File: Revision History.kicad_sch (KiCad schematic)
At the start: 0 parts

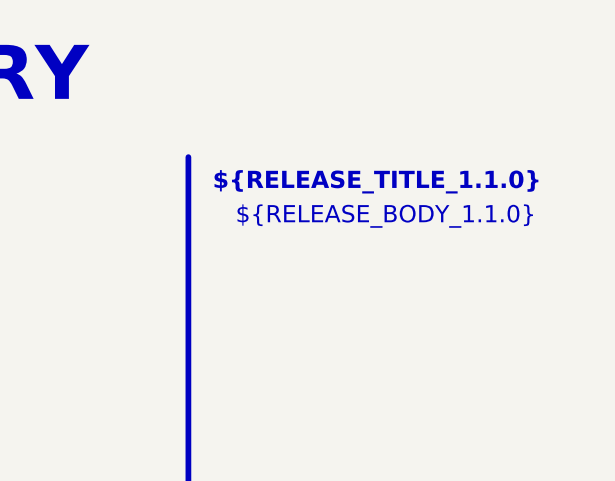
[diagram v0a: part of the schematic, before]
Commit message: fix: improved crystal oscillator layout
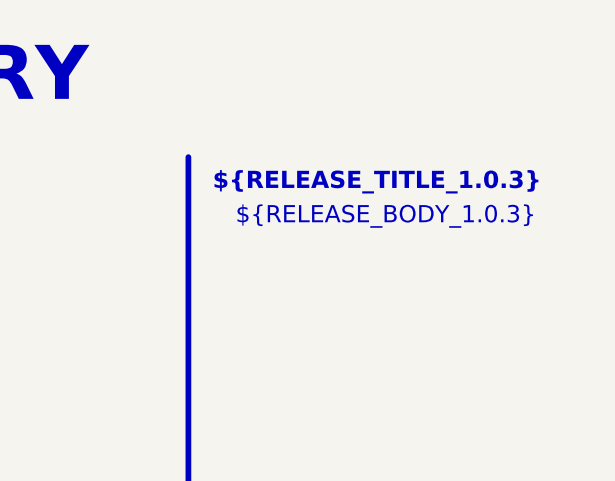
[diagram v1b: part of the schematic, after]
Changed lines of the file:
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@@
 		(company "${COMPANY}")
 	)
-	(text_box "${RELEASE_BODY_1.1.0}"
+	(text_box "${RELEASE_BODY_1.0.3}"
 		(exclude_from_sim no)
 		(at 224.79 35.56 0)
@@
 		(stroke
 			(width -0.0001)
-			(type default)
+			(type solid)
 		)
 		(fill
@@
 		)
 	)
-	(text_box "${RELEASE_TITLE_1.1.0}"
+	(text_box "${RELEASE_TITLE_1.0.3}"
 		(exclude_from_sim no)
 		(at 222.25 31.75 0)
@@
 		(stroke
 			(width -0.0001)
-			(type default)
+			(type solid)
 		)
 		(fill

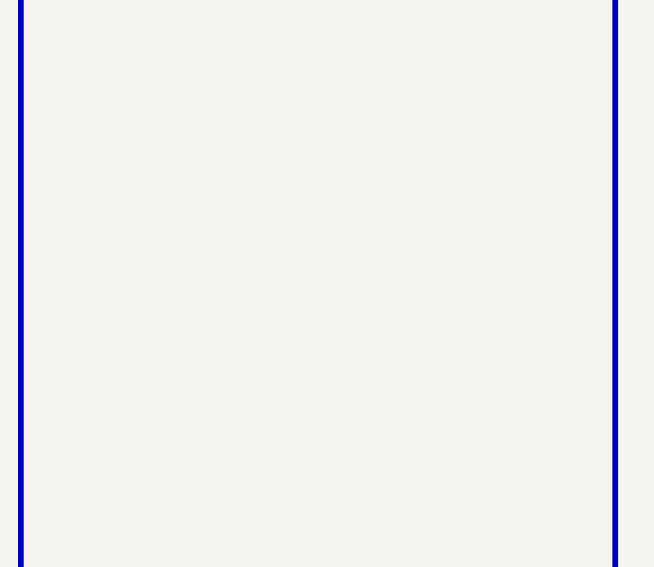
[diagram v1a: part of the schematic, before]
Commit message: fix: add ground pour under uC
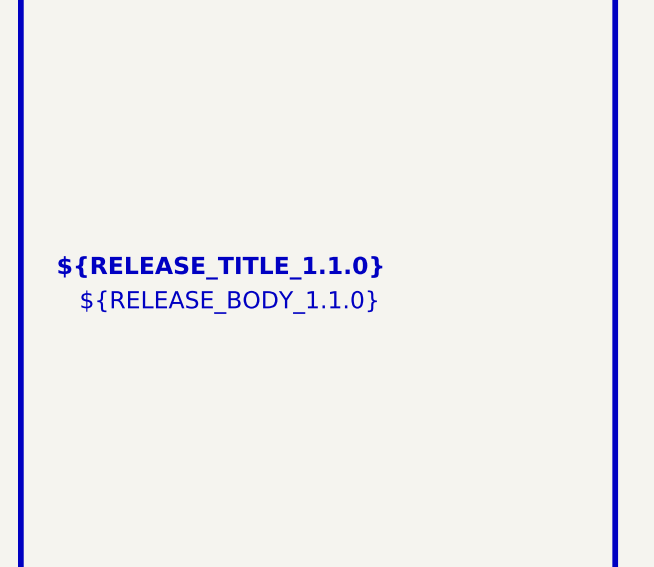
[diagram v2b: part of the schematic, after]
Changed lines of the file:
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@@
+		)
+	)
+	(text_box "${RELEASE_TITLE_1.1.0}"
+		(exclude_from_sim no)
+		(at 25.4 67.31 0)
+		(size 57.15 7.62)
+		(margins 1.4287 1.4287 1.4287 1.4287)
+		(stroke
+			(width -0.0001)
+			(type solid)
+		)
+		(fill
+			(type none)
+		)
+		(effects
+			(font
+				(face "Arial")
+				(size 1.905 1.905)
+				(thickness 0.254)
+				(bold yes)
+			)
+			(justify left top)
 		)
 	)
@@
 		(exclude_from_sim no)
 		(at 26.67 35.56 0)
-		(size 58.42 146.05)
+		(size 58.42 29.21)
 		(margins 1.4287 1.4287 1.4287 1.4287)
 		(stroke
@@
 		)
 		(fill
+			(type none)
+		)
+		(effects
+			(font
+				(face "Arial")
+				(size 1.905 1.905)
+				(color 0 0 0 1)
+			)
+			(justify left top)
+		)
+	)
+	(text_box "${RELEASE_BODY_1.1.0}"
+		(exclude_from_sim no)
+		(at 27.94 71.12 0)
+		(size 58.42 29.21)
+		(margins 1.4287 1.4287 1.4287 1.4287)
+		(stroke
+			(width -0.0001)
+			(type solid)
+		)
+		(fill

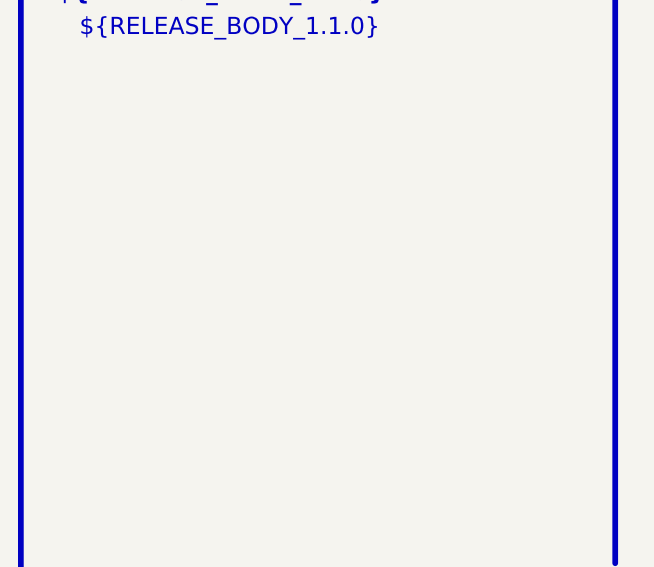
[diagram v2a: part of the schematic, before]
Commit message: fix: circuit schem as one sheet
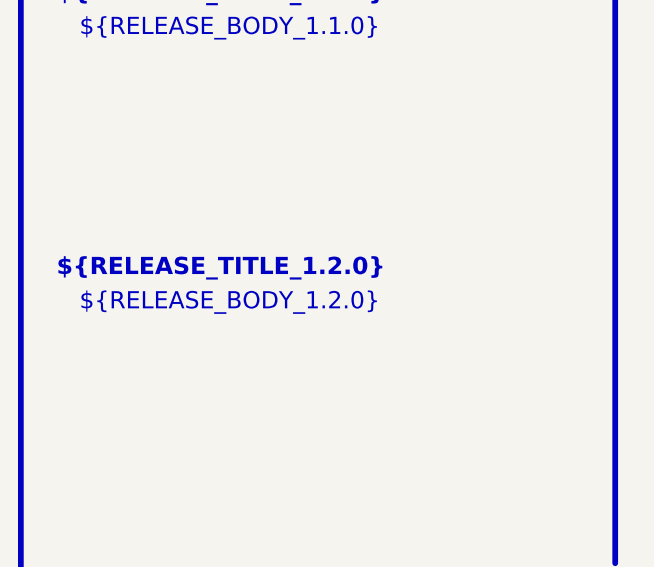
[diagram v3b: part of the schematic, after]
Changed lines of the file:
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@@
 	(title_block
 		(title "REVISION HISTORY")
-		(date "2026-04-06")
+		(date "2026-05-09")
 		(rev "${REVISION}")
 		(company "${COMPANY}")
@@
 		)
 	)
+	(text_box "${RELEASE_TITLE_1.2.0}"
+		(exclude_from_sim no)
+		(at 25.4 97.79 0)
+		(size 57.15 7.62)
+		(margins 1.4287 1.4287 1.4287 1.4287)
+		(stroke
+			(width -0.0001)
+			(type solid)
+		)
+		(fill
+			(type none)
+		)
+		(effects
+			(font
+				(face "Arial")
+				(size 1.905 1.905)
+				(thickness 0.254)
+				(bold yes)
+			)
+			(justify left top)
+		)
+	)
 	(text_box "${RELEASE_BODY_1.0.2}"
 		(exclude_from_sim no)
@@
 		(size 58.42 29.21)
 		(margins 1.4287 1.4287 1.4287 1.4287)
+		(stroke
+			(width -0.0001)
+			(type solid)
+		)
+		(fill
+			(type none)
+		)
+		(effects
+			(font
+				(face "Arial")
+				(size 1.905 1.905)
+				(color 0 0 0 1)
+			)
+			(justify left top)
+		)
+	)
+	(text_box "${RELEASE_BODY_1.2.0}"
+		(exclude_from_sim no)
+		(at 27.94 101.6 0)
+		(size 58.42 29.21)
+		(margins 1.4287 1.4287 1.4287 1.4287)
